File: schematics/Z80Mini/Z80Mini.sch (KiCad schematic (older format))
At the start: 31 parts, among them J1 Conn_02x20_Odd_Even, J2 TTL Serial, Q1 BC337, SW1 RESET, U1 Z80CPU, U2 TC55257CPI, U3 28C256, U4 NE555, U5 74HC14, U6 74LS139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

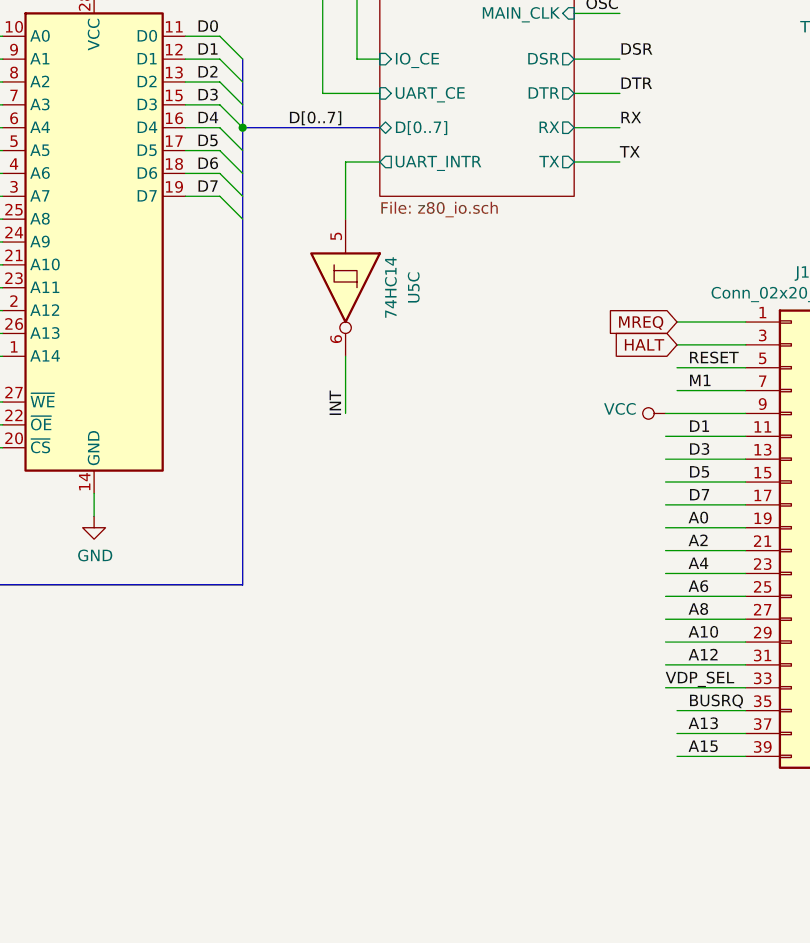
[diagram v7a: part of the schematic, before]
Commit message: Changed some parts of code and added new hardware module to emulate IM 2 and vector interrpt without Z80 dasy chain
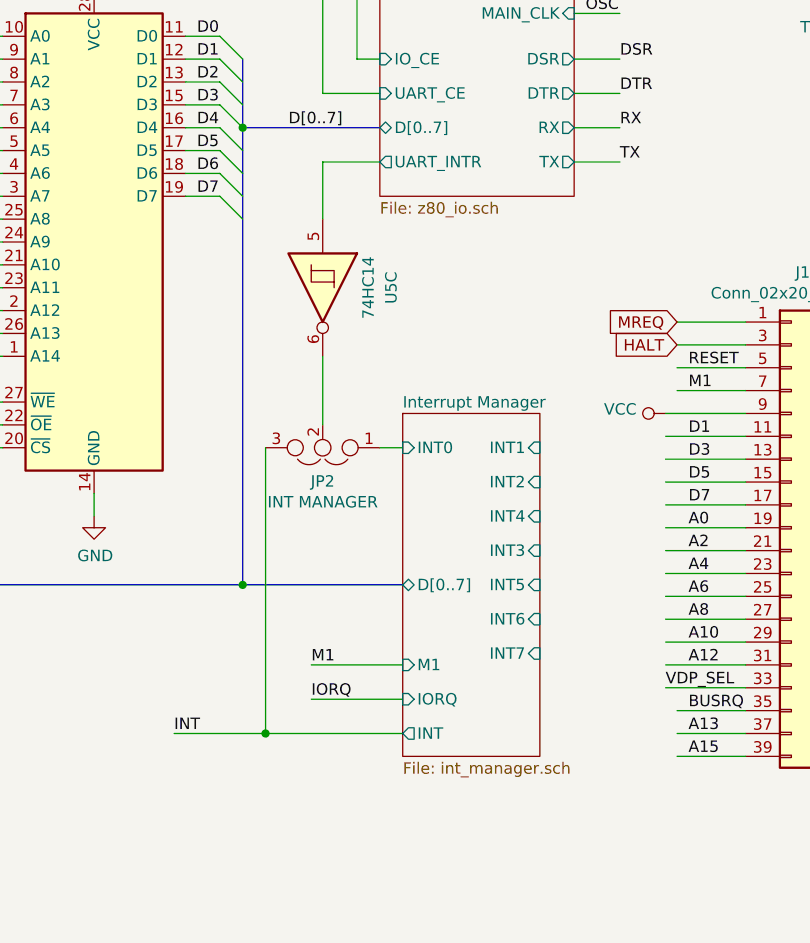
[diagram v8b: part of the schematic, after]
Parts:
- added JP2: INT MANAGER, symbol Device:Jumper_NC_Dual
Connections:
- wire segments 269 -> 275
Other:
- moved on the sheet: U5C
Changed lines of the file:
@@
 $Descr A4 11693 8268
 encoding utf-8
-Sheet 1 2
+Sheet 1 3
 Title ""
 Date ""
@@
 	0    -1   -1   0
 $EndComp
-Wire Wire Line
-	7950 3450 7950 3200
 Entry Wire Line
 	6150 3950 6250 4050
@@
 Wire Wire Line
 	6650 1150 6350 1150
-Wire Wire Line
-	7950 4050 7950 4300
 Wire Bus Line
 	4250 5050 5650 5050
@@
 Text Label 7650 1850 0    50   ~ 0
 A[0..15]
-Text Label 7950 4200 3    50   ~ 0
-INT
 Text Label 5500 3950 0    50   ~ 0
 D3
@@
 Wire Bus Line
 	7500 3050 8100 3050
-Wire Wire Line
-	8100 3200 7950 3200
 Wire Wire Line
 	7750 1350 8750 1350
@@
 L 74xx:74HC14 U5
 U 3 1 5DB892B7
-P 7950 3750
-F 0 "U5" H 7950 4050 50  0000 C CNN
-F 1 "74HC14" H 7950 3950 50  0000 C CNN
-F 2 "Package_DIP:DIP-14_W7.62mm_LongPads" H 7950 3750 50  0001 C CNN
-F 3 "http://www.ti.com/lit/gpn/sn74HC14" H 7950 3750 50  0001 C CNN
-	3    7950 3750
+P 7850 3750
+F 0 "U5" H 7850 4050 50  0000 C CNN
+F 1 "74HC14" H 7850 3950 50  0000 C CNN
+F 2 "Package_DIP:DIP-14_W7.62mm_LongPads" H 7850 3750 50  0001 C CNN
+F 3 "http://www.ti.com/lit/gpn/sn74HC14" H 7850 3750 50  0001 C CNN
+	3    7850 3750
 	0    1    1    0
 $EndComp
@@
 Wire Wire Line
 	5350 6500 5500 6500
+$Sheet
+S 8200 4300 600  1500
+U 62BC9CCB
+F0 "Interrupt Manager" 50
+F1 "int_manager.sch" 50
+F2 "INT0" I L 8200 4450 50
+F3 "INT" O L 8200 5700 50
+F4 "D[0..7]" B L 8200 5050 50
+F5 "INT1" I R 8800 4450 50
+F6 "INT2" I R 8800 4600 50
+F7 "INT4" I R 8800 4750 50
+F8 "INT5" I R 8800 5050 50
+F9 "IORQ" I L 8200 5550 50
+F10 "M1" I L 8200 5400 50
+F11 "INT6" I R 8800 5200 50
+F12 "INT7" I R 8800 5350 50
+F13 "INT3" I R 8800 4900 50
+$EndSheet
+$Comp
+L Device:Jumper_NC_Dual JP2
+U 1 1 62BCB640
+P 7850 4450
+F 0 "JP2" H 7850 4597 50  0000 C CNN
+F 1 "INT MANAGER" H 7850 4688 50  0000 C CNN
+F 2 "" H 7850 4450 50  0001 C CNN
+F 3 "~" H 7850 4450 50  0001 C CNN
+	1    7850 4450
+	-1   0    0    1
+$EndComp
+Wire Wire Line
+	8100 3200 7850 3200
+Wire Wire Line
+	7850 3200 7850 3450
+Wire Wire Line
+	7850 4050 7850 4350
+Wire Wire Line
+	8100 4450 8200 4450
+Wire Wire Line
+	7600 4450 7600 5700
+Wire Wire Line
+	7600 5700 7200 5700
+Wire Wire Line
+	8200 5700 7600 5700
+Connection ~ 7600 5700
+Text Label 7200 5700 0    50   ~ 0
+INT
+Wire Bus Line
+	8200 5050 7500 5050
+Connection ~ 7500 5050
+Wire Wire Line
+	8200 5550 7800 5550
+Wire Wire Line
+	8200 5400 7800 5400
 Wire Bus Line
 	4250 3750 4250 5050
@@
 Wire Bus Line
 	6150 1850 6150 3950
+Text Label 7800 5400 0    50   ~ 0
+M1
+Text Label 7800 5550 0    50   ~ 0
+IORQ
 $EndSCHEMATC
